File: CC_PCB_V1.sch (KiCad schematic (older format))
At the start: 7 parts, among them J2 Antenna_Conn_02x04_Odd_Even, J3 USB1130-15-A_REVA, J5 Relay_Conn_01x06, U1 Pico

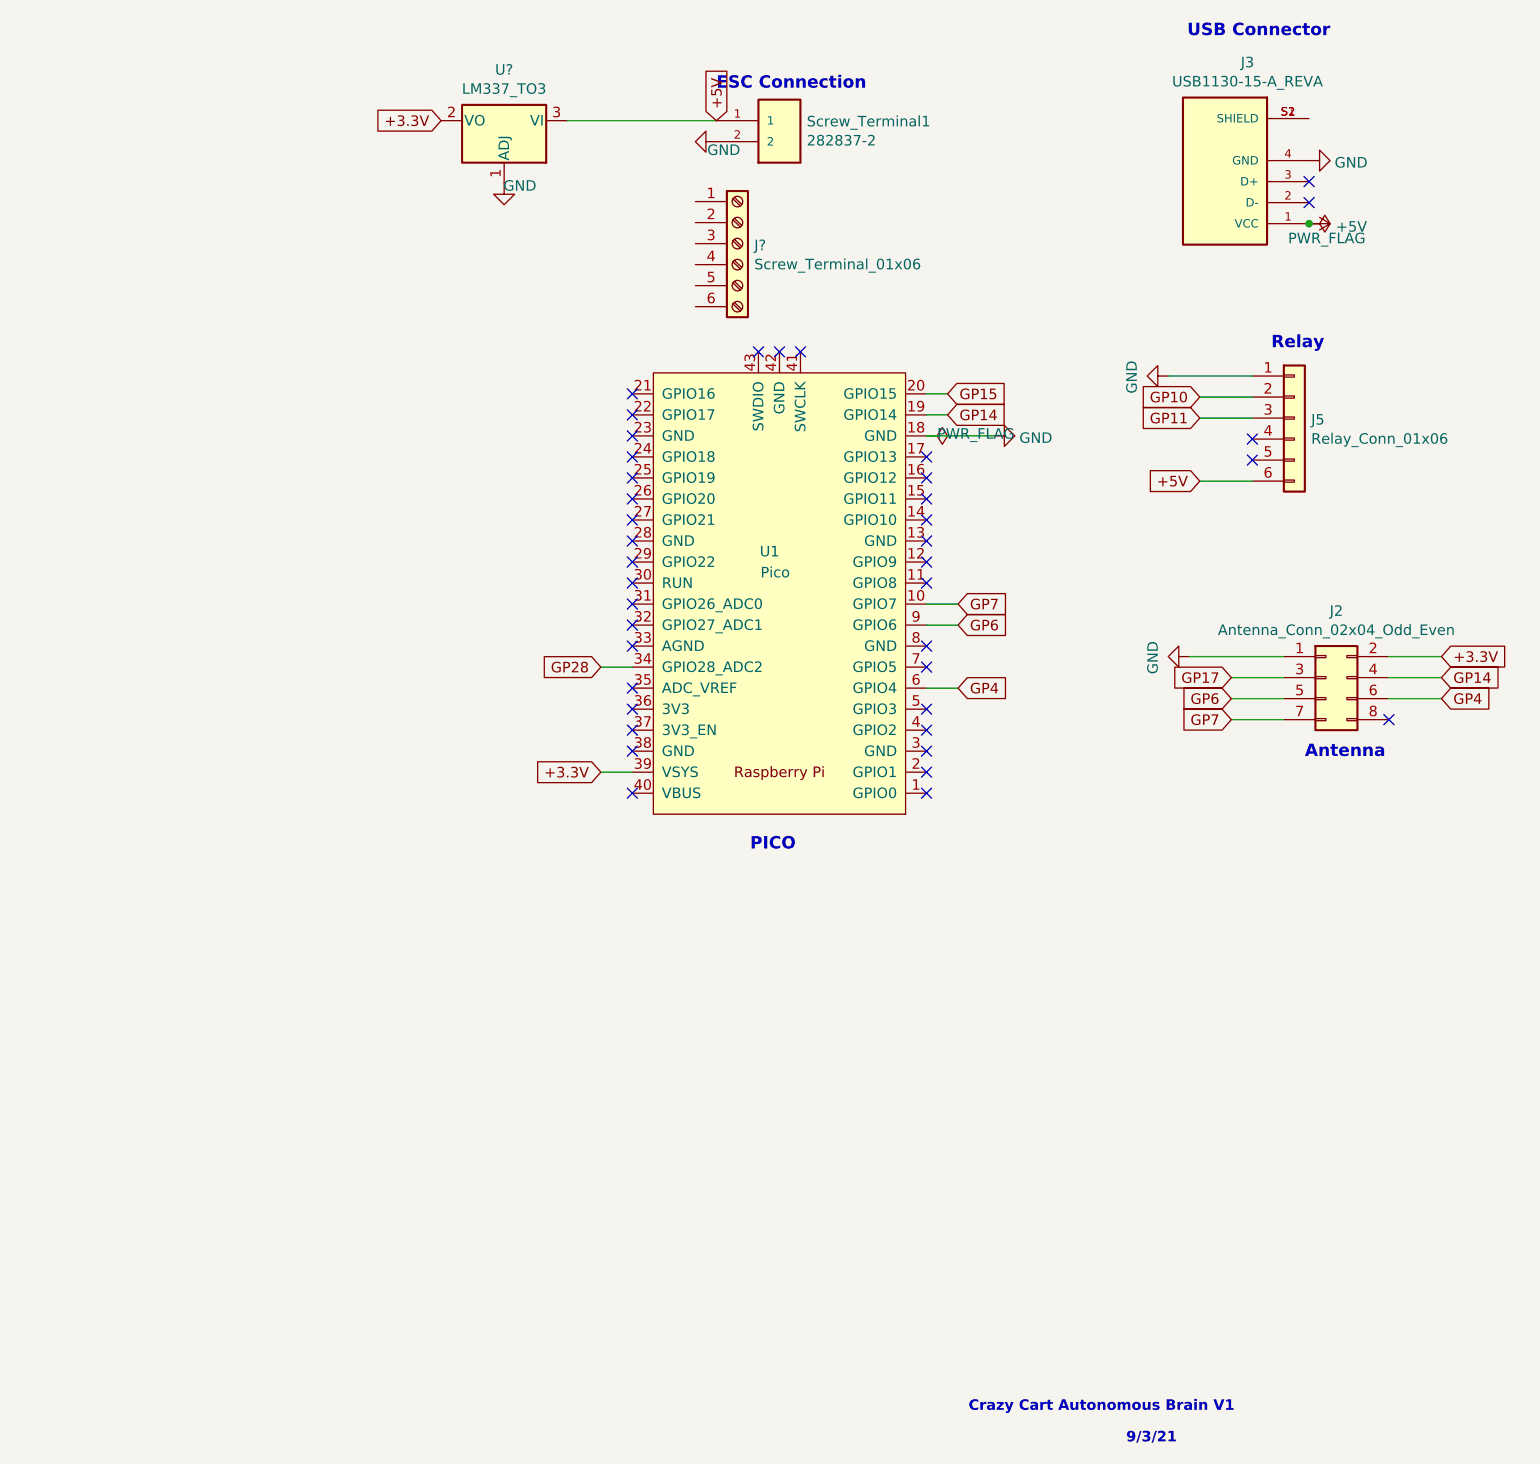
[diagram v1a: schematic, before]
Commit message: Finished SCH and added components to PCB
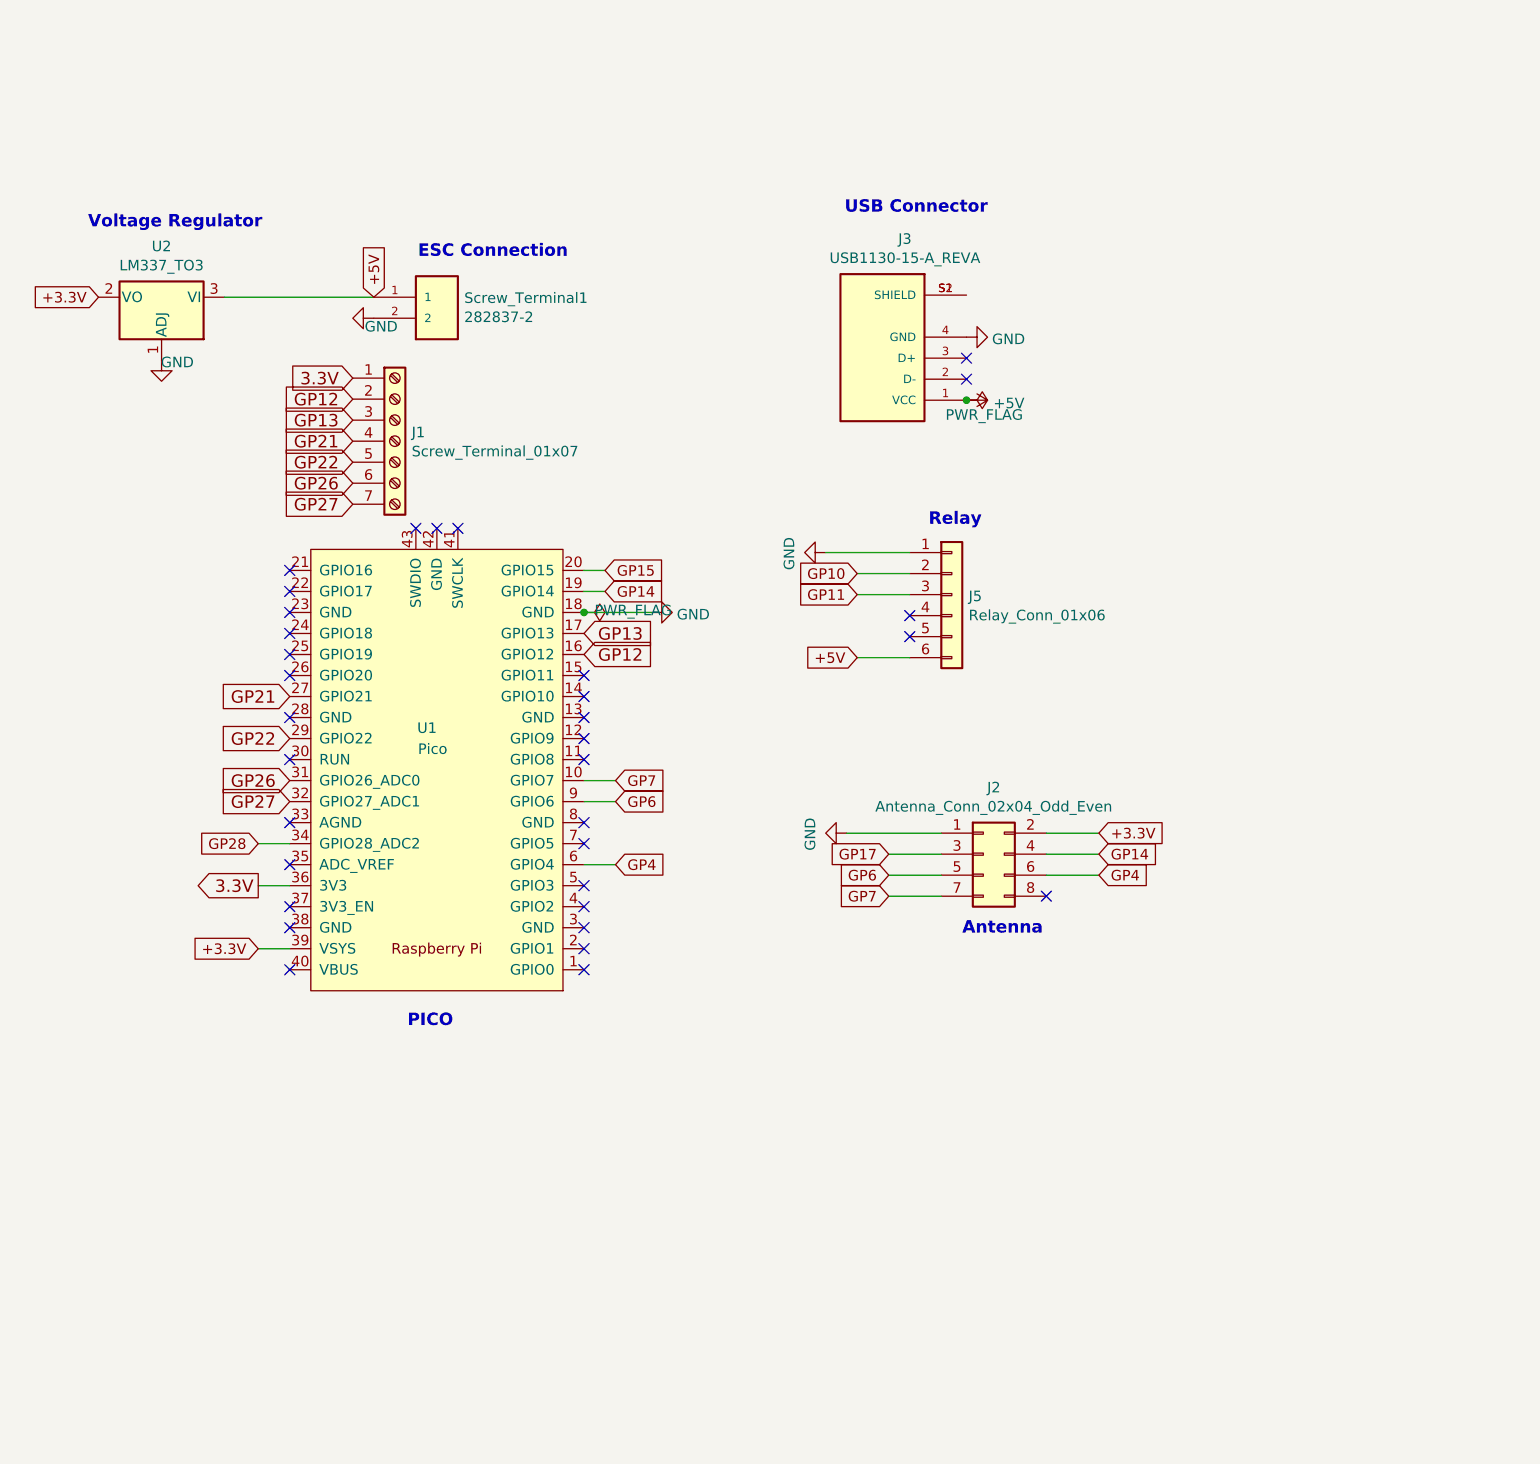
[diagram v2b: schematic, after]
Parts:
- removed J?: Screw_Terminal_01x06, symbol Connector:Screw_Terminal_01x06
- added J1: Screw_Terminal_01x07, TerminalBlock_TE-Connectivity:TerminalBlock_TE_282834-7_1x07_P2.54mm_Horizontal, symbol Connector:Screw_Terminal_01x07
- U2: renamed from U?; footprint Package_TO_SOT_THT:TO-3 -> MCU_RaspberryPi_and_Boards:TO254P1054X470X1955-3
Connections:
- net GP12: now reaches U1.16 (GPIO12)
- net GP12: now also J1.2 (Pin_2)
- net GP13: now reaches U1.17 (GPIO13)
- net GP13: now also J1.3 (Pin_3)
- net GP21: now reaches U1.27 (GPIO21)
- net GP21: now also J1.4 (Pin_4)
- net GP22: now reaches U1.29 (GPIO22)
- net GP22: now also J1.5 (Pin_5)
- net GP26: now reaches U1.31 (GPIO26_ADC0)
- net GP26: now also J1.6 (Pin_6)
- net GP27: now reaches U1.32 (GPIO27_ADC1)
- net GP27: now also J1.7 (Pin_7)
- net 3.3V: now reaches U1.36 (3V3)
- net 3.3V: now also J1.1 (Pin_1)
- no-connect marks 40 -> 33
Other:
- note added: "Voltage Regulator"
- note removed: "9/3/21\n"
- note removed: "Crazy Cart Autonomous Brain V1\n"
- moved on the sheet: J2, J3, J5, Screw_Terminal1, U1, U2
